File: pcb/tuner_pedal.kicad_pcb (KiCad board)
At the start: 4 copper layers, 50 x 100 mm, 104 parts, among them J1 9V Battery, J2 9V Barrel Female, J3 UART, J4 Fermion 1.8" TFT LCD, J5 SWD, J6 Potentiometer, J7 Guitar Input, J8 Guitar Output, SW1 NRST, SW2 BOOT0, U1 TPS54302, U2 MCP1700T-3302E/TT, U3 PCM1802DB, U4 STM32F411CEU6, U5 TL072, X1 4.096MHz, Y1 25MHz 9pF

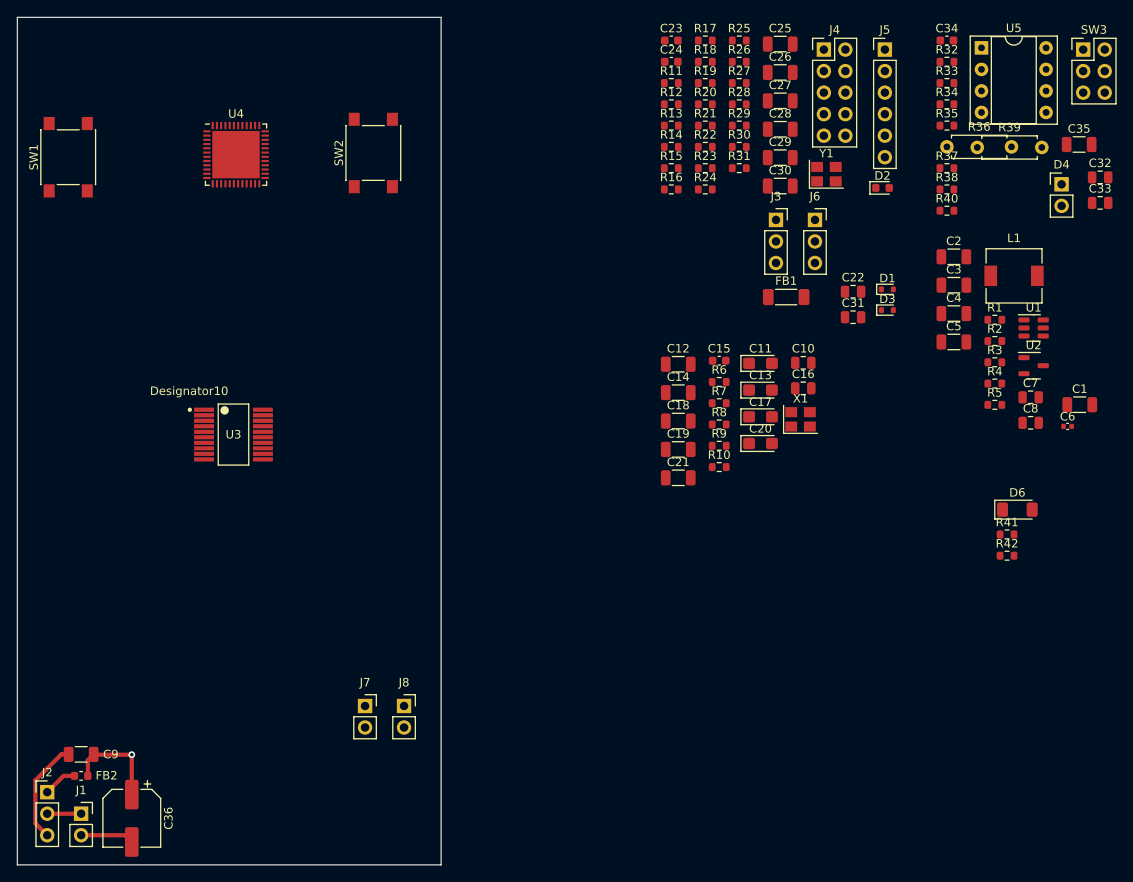
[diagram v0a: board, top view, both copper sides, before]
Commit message: Added Analog in signal and 9V to 5V buck converter
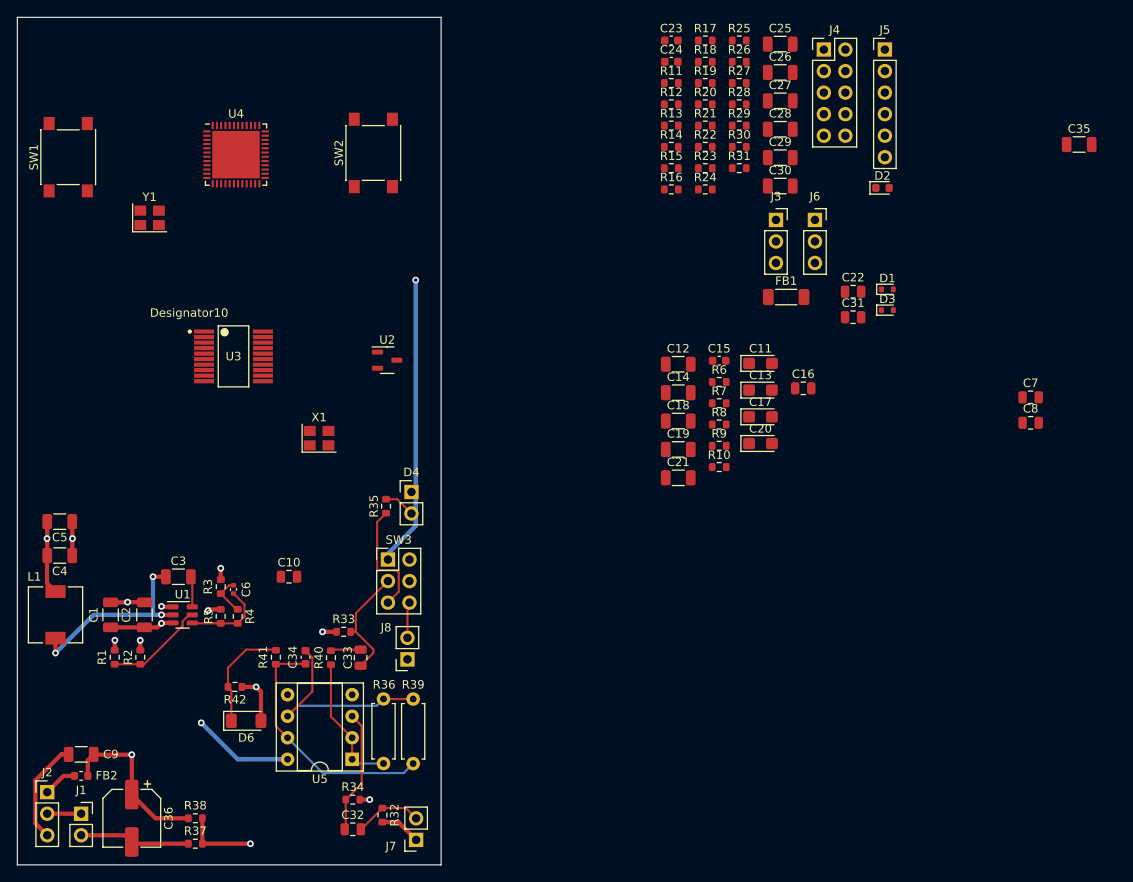
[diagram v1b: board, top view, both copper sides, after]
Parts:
- moved L1 120.0 mm to (115.5, 103.5), turned to 90 degrees
- moved R37 119.2 mm to (132.0, 130.5), turned to 180 degrees
- moved C32 117.0 mm to (150.6, 128.8)
- moved C1 117.0 mm to (122.0, 103.5), turned to 90 degrees
- moved R38 115.6 mm to (132.0, 127.5)
- moved U5 112.1 mm to (150.5, 120.5), turned to 180 degrees
- moved R1 111.2 mm to (122.5, 108.5), turned to -90 degrees
- moved R32 111.1 mm to (154.1, 127.1), turned to -90 degrees
- moved C4 109.3 mm to (116.0, 96.5), turned to 180 degrees
- moved R34 107.9 mm to (150.6, 125.3)
- moved C5 107.6 mm to (116.0, 92.5), turned to 180 degrees
- moved R2 107.5 mm to (125.5, 108.5), turned to 90 degrees
- moved U1 106.0 mm to (130.5, 103.5)
- moved C34 105.0 mm to (145.0, 108.5), turned to -90 degrees
- moved C2 104.4 mm to (126.0, 103.5), turned to -90 degrees
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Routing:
- net +3.3V: track 0.00 -> 34.3 mm, vias 0 -> 1
- net GND: track 19.0 -> 50.3 mm, vias 0 -> 7
- net Net-(C34-Pad2): track 0.00 -> 29.8 mm
- net +9VA: track 12.0 -> 40.6 mm, vias 1 -> 4
- net Net-(U5B--): track 0.00 -> 25.0 mm
- net Net-(U1-SW): track 0.00 -> 24.0 mm, vias 0 -> 3
- net /Analog Signal/buffered_in: track 0.00 -> 16.1 mm
- net Net-(U5A-+): track 0.00 -> 14.6 mm
- net Net-(R35-Pad1): track 0.00 -> 13.9 mm
- net Net-(C33-Pad2): track 0.00 -> 13.6 mm
- net /ADC/V_{IN}: track 0.00 -> 13.0 mm
- net Net-(U1-EN): track 0.00 -> 11.9 mm
- net +5VA: track 0.00 -> 10.0 mm, vias 0 -> 2
- net /Analog Signal/+4V5: track 0.00 -> 9.85 mm, vias 0 -> 2
- net Net-(U1-FB): track 0.00 -> 9.77 mm
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- added copper zone on In2.Cu, net /Analog Signal/+4V5

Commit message: First revision of the pcb layout
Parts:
- removed R30, R31: 10k, Resistor_SMD:R_0603_1608Metric
- added 3V3: TestPoint_Pad_D1.5mm, TestPoint:TestPoint_Pad_D1.5mm, F.Cu at (147.3, 68.6)
- added 4V5: TestPoint_Pad_D1.5mm, TestPoint:TestPoint_Pad_D1.5mm, F.Cu at (137.5, 99.5)
- added 5V: TestPoint_Pad_D1.5mm, TestPoint:TestPoint_Pad_D1.5mm, F.Cu at (152.4, 68.6)
- added 9V: TestPoint_Pad_D1.5mm, TestPoint:TestPoint_Pad_D1.5mm, F.Cu at (133.5, 99.5)
- added GND: TestPoint_Pad_D1.5mm, TestPoint:TestPoint_Pad_D1.5mm, F.Cu at (149.9, 73.7)
- C12, C14, C18, C19, C2, C21, C25, C26, C27, C28, C29, C3, C30, C35, C9: footprint Capacitor_SMD:C_1206_3216Metric -> Capacitor_SMD:C_0402_1005Metric
- C23, C24, C34: footprint Capacitor_SMD:C_0603_1608Metric -> Capacitor_SMD:C_0402_1005Metric
- U3: footprint pcm1802:DB0020A-IPC_A -> Package_SO:SSOP-20_5.3x7.2mm_P0.65mm
- moved C35 116.7 mm to (140.5, 114.6), turned to -90 degrees
- moved C8 115.8 mm to (115.5, 68.1)
- moved C7 115.1 mm to (115.5, 75.1)
- moved D2 99.8 mm to (113.5, 60.0), turned to -90 degrees
- moved J5 98.0 mm to (115.3, 36.5), turned to 90 degrees
- moved J6 91.0 mm to (115.5, 41.0), turned to 90 degrees
- moved C31 86.0 mm to (126.0, 48.5), turned to 90 degrees
- moved C20 80.2 mm to (118.5, 85.3), turned to 180 degrees
- moved FB1 79.0 mm to (124.0, 52.0)
- moved C22 72.0 mm to (138.0, 58.0), turned to 90 degrees
- moved C27 71.8 mm to (129.5, 49.0), turned to 180 degrees
- moved D1 71.7 mm to (145.8, 42.0), turned to 180 degrees
- moved R16 70.7 mm to (117.5, 56.0), turned to 180 degrees
- moved C29 70.5 mm to (130.5, 50.5), turned to 180 degrees
- moved R14 70.0 mm to (119.8, 63.3)
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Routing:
- net +3.3V: track 34.3 -> 144.3 mm, vias 1 -> 16
- net GND: track 50.3 -> 141.8 mm, vias 7 -> 46
- net /MCU/Display_BL: track 0.00 -> 62.9 mm, vias 0 -> 1
- net /MCU/active_tuning: track 0.00 -> 58.6 mm, vias 0 -> 3
- net /MCU/Display_RT: track 0.00 -> 54.8 mm, vias 0 -> 1
- net /MCU/Display_DC: track 0.00 -> 54.7 mm, vias 0 -> 1
- net /MCU/Display_CS: track 0.00 -> 52.7 mm, vias 0 -> 1
- net /MCU/NRST: track 0.00 -> 46.3 mm, vias 0 -> 3
- net /MCU/SWDIO: track 0.00 -> 35.6 mm, vias 0 -> 2
- net /MCU/BOOT0: track 0.00 -> 35.3 mm, vias 0 -> 2
- net /MCU/I2S1_WS: track 0.00 -> 34.5 mm
- net /MCU/GPIO_LED: track 0.00 -> 31.4 mm, vias 0 -> 2
- net /MCU/I2S1_CK: track 0.00 -> 28.9 mm
- net /MCU/I2S1_SD: track 0.00 -> 28.5 mm
- net /MCU/SWCLK: track 0.00 -> 28.0 mm, vias 0 -> 2
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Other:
- board size 50 x 100 mm -> 50 x 90 mm
- board text added: "Tuner Pedal"

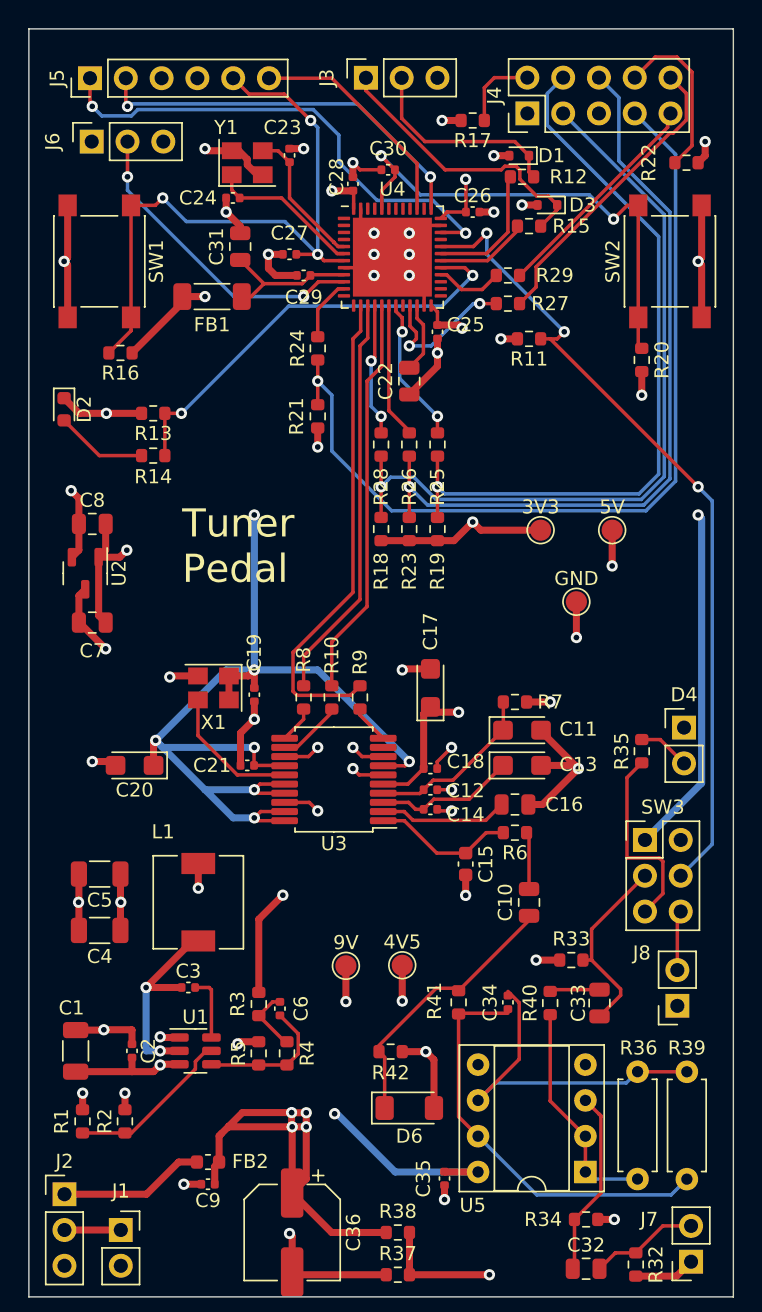
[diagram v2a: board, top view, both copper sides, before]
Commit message: trying to isolate analog from noise sources
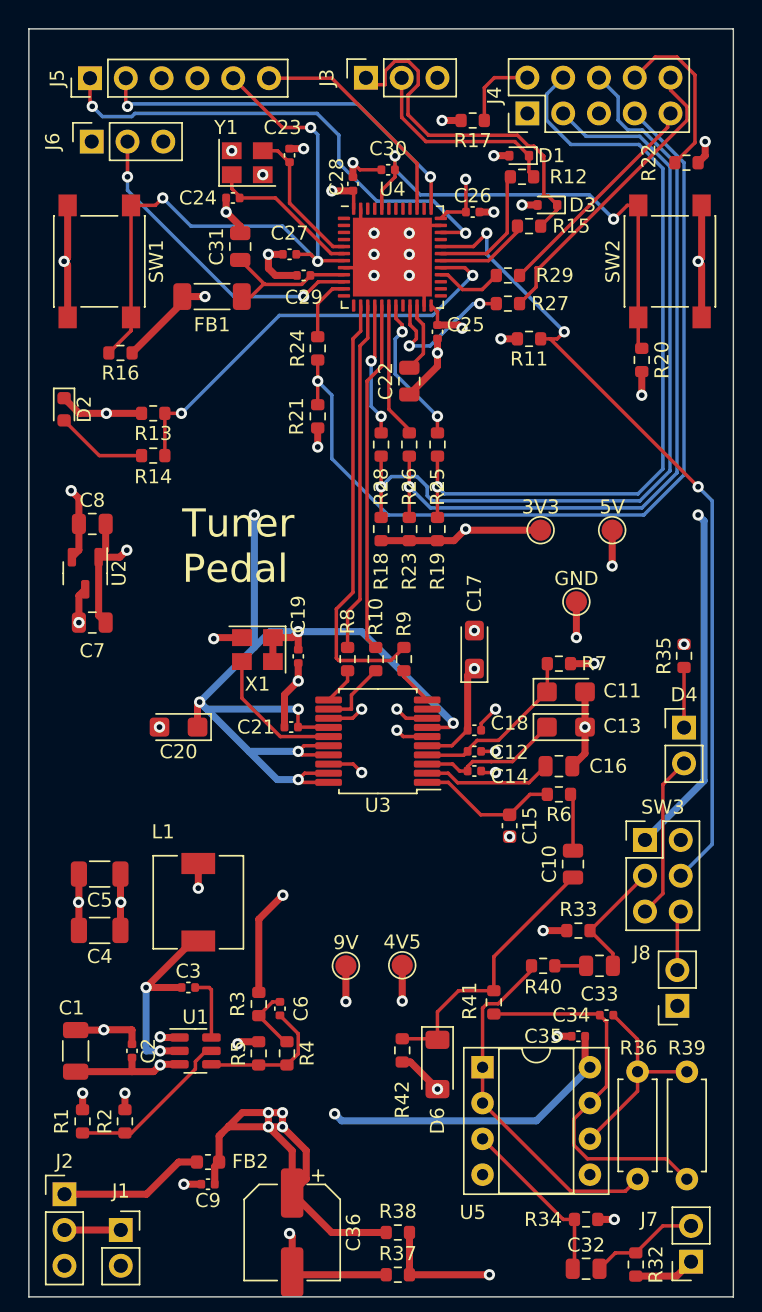
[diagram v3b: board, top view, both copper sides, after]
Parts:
- moved C35 13.9 mm to (150.0, 104.5), turned to 180 degrees
- moved U5 10.4 mm to (143.2, 106.7), turned to 0 degrees
- moved R35 7.40 mm to (157.5, 77.5)
- moved C34 7.06 mm to (152.0, 103.0), turned to 180 degrees
- moved C10 4.14 mm to (149.6, 92.3)
- moved C11 4.14 mm to (149.1, 80.1)
- moved C12 4.14 mm to (142.6, 84.3)
- moved C13 4.14 mm to (149.1, 82.6)
- moved C14 4.14 mm to (142.6, 85.7)
- moved C15 4.14 mm to (145.1, 89.6)
- moved C16 4.14 mm to (148.6, 85.3)
- moved C17 4.14 mm to (142.6, 77.1)
- moved C18 4.14 mm to (142.6, 82.8)
- moved C19 4.14 mm to (130.1, 77.5)
- moved C20 4.14 mm to (121.6, 82.6)
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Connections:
- D4 pad 1: GND -> Net-(D4-K)
- R35 pad 1: Net-(R35-Pad1) -> Net-(D4-K)
- R35 pad 2: Net-(D4-A) -> GND
- SW3 pad 5: Net-(R35-Pad1) -> Net-(D4-A)
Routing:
- net GND: track 141.8 -> 123.3 mm, vias 46 -> 48
- net Net-(R35-Pad1): track 13.9 -> 0.00 mm
- net Net-(U5B--): track 24.9 -> 14.4 mm
- net /Analog Signal/buffered_in: track 16.1 -> 25.6 mm
- net Net-(D4-A): track 3.70 -> 11.7 mm
- net +9VA: track 62.3 -> 68.2 mm
- net /MCU/USART1_TX: track 20.4 -> 25.8 mm
- net Net-(C33-Pad2): track 13.6 -> 8.53 mm
- net +5VA: track 32.9 -> 28.0 mm
- net Net-(D4-K): track 0.00 -> 4.27 mm
- net /MCU/I2S1_CK: track 28.9 -> 24.9 mm
- net /MCU/I2S1_WS: track 34.5 -> 31.0 mm
- net /MCU/I2S1_SD: track 28.5 -> 25.0 mm
- net /MCU/Display_CS: track 52.7 -> 55.8 mm
- net /MCU/Display_RT: track 54.8 -> 57.9 mm
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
